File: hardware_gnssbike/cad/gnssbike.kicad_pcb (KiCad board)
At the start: 4 copper layers, 34 x 90 mm, 134 parts, among them J101 HRO TYPE-C-31-M-12, J102 JST SM06B-GHS-TB, J103 JST S4B-ZR-SM4A-TF, J201 Tag-Connect TC2030-NL, J302 Hirose U.FL-R-SMT-1, J401 Hirose FH12-10S-0.5SH(55), J402 Molex 503480-0500, Q401 DMG1012T-7, Q601 DMG1012T-7, Q602 DMG1012T-7, Q603 DMG1012T-7, SW601 XunPu TS-1088R-02026, SW602 XunPu TS-1088R-02026, SW603 XunPu TS-1088R-02026, U101 nPM1300-QEAA, U102 MAX17262REWL, U103 AEM10900, U104 TPS7A0218PDQN, U201 MinewSemi ME54BS13, U301 u-blox MAX-F10S, U302 TI TXU0204BQAR, U501 MX25R6435F, U502 Bosch BMP585, U503 Bosch BMI270, U504 Memsic MMC5603NJ, U505 TI OPT3001DNPR

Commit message: fix(hardware): the antenna cut-out follows the drawing, and the board says which way round
The cut-out was 20,08 mm wide because the data sheet's 15,00 is
asymmetric about the antenna - 2,46 mm one side, 7,54 the other - and
which side was which had not been determined, so 7,54 went on both.

It has now been determined, by measuring the drawings rather than by
reading a line of text, because the data sheet never states it: the wide
side is the side of the "U" printed on top. The "U" is off-centre by
1,10 mm, 22 % of the part's length, and falls on the portion facing the
wide cut-out in two independent figures - the dimension drawing and the
evaluation board. The asymmetry is deliberate: on the 80 x 40 mm
evaluation board the cut-out sits in the middle, 30 mm from one side
edge and 35 from the other, so there was room to centre it and Unictron
did not.

So the cut-out goes back to 15,00 mm, with the wide side toward +x. The
board gets back the 5 mm of ground plane it was giving away, on an
antenna that was already going to sit below its 80 x 40 mm reference
plane. The two strips of copper left in that band are 8,3 and 10,7 mm
instead of 3,2 and 15,9.

And the footprint now carries an orientation mark, which is not
decoration. The part is PHYSICALLY SYMMETRIC - both end terminations are
identical wrap-arounds and the signal terminal is at the geometric
centre - so pick-and-place cannot tell the orientation from the
geometry, and a part placed 180 degrees out puts the wrong side into the
wide cut-out and PASSES every electrical test, because electrically the
two ends are the same. A filled arrow and a "U" on the silkscreen say
which way the logo has to point.

Two things stay open, and both are recorded rather than guessed: the
"U" is Unictron's logo and the data sheet does not declare it as an
orientation mark, so this is a reading of figures; and the data sheet
has no minimum keep-out note at all, referring instead to an application
note, "General guidelines for the 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
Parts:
- moved U302 15.4 mm to (31.5, 33.0)
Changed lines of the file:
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@@
 		(polygon
 			(pts
-				(xy 28.2100 25.0000)
+				(xy 33.2900 25.0000)
 				(xy 48.2900 25.0000)
 				(xy 48.2900 34.8800)
-				(xy 28.2100 34.8800)
+				(xy 33.2900 34.8800)
 			)
 		)
@@
 		(roundrect_rratio 0.25)
 	)
+	(fp_poly
+		(pts (xy 3.10 -1.90) (xy 4.00 -1.40) (xy 3.10 -0.90))
+		(stroke (width 0.12) (type solid))
+		(fill solid)
+		(layer "F.SilkS")
+	)
+	(fp_text user "U"
+		(at 2.20 -2.40 0)
+		(layer "F.SilkS")
+		(effects (font (size 0.6 0.6) (thickness 0.12)))
+	)
 	(model "${KIPRJMOD}/3d/Antena_Unictron_H2UJ4U1H2Q0100_5x3mm.wrl"
 		(offset (xyz 0 0 0))
@@
 		(at 41.5000 35.5000 0)
 		(property "Reference" "JP301"
-			(at 0.0000 -1.1000 0)
+			(at 0.0000 1.1000 0)
 			(layer "F.SilkS")
 			(effects (font (size 0.6 0.6) (thickness 0.12)))
@@
 		(at 40.8000 40.2000 90)
 		(property "Reference" "L301"
-			(at 2.4020 -0.0000 90)
+			(at -0.0000 -1.1500 90)
 			(layer "F.SilkS")
 			(effects (font (size 0.6 0.6) (thickness 0.12)))
@@
 		(at 33.5000 40.3000 180)
 		(property "Reference" "U301"
-			(at 0.0000 5.8000 0)
+			(at -7.1720 5.8000 0)
 			(layer "F.SilkS")
 			(effects (font (size 0.6 0.6) (thickness 0.12)))
@@
 	(footprint "gnssbike:TXU0204_WQFN-14_3x2.5mm_P0.5mm"
 		(layer "F.Cu")
-		(at 44.0000 42.0000 0)
+		(at 31.5000 33.0000 0)
 		(property "Reference" "U302"
-			(at 0.0000 2.1400 0)
+			(at 0.0000 -2.1400 0)
 			(layer "F.SilkS")
 			(effects (font (size 0.6 0.6) (thickness 0.12)))

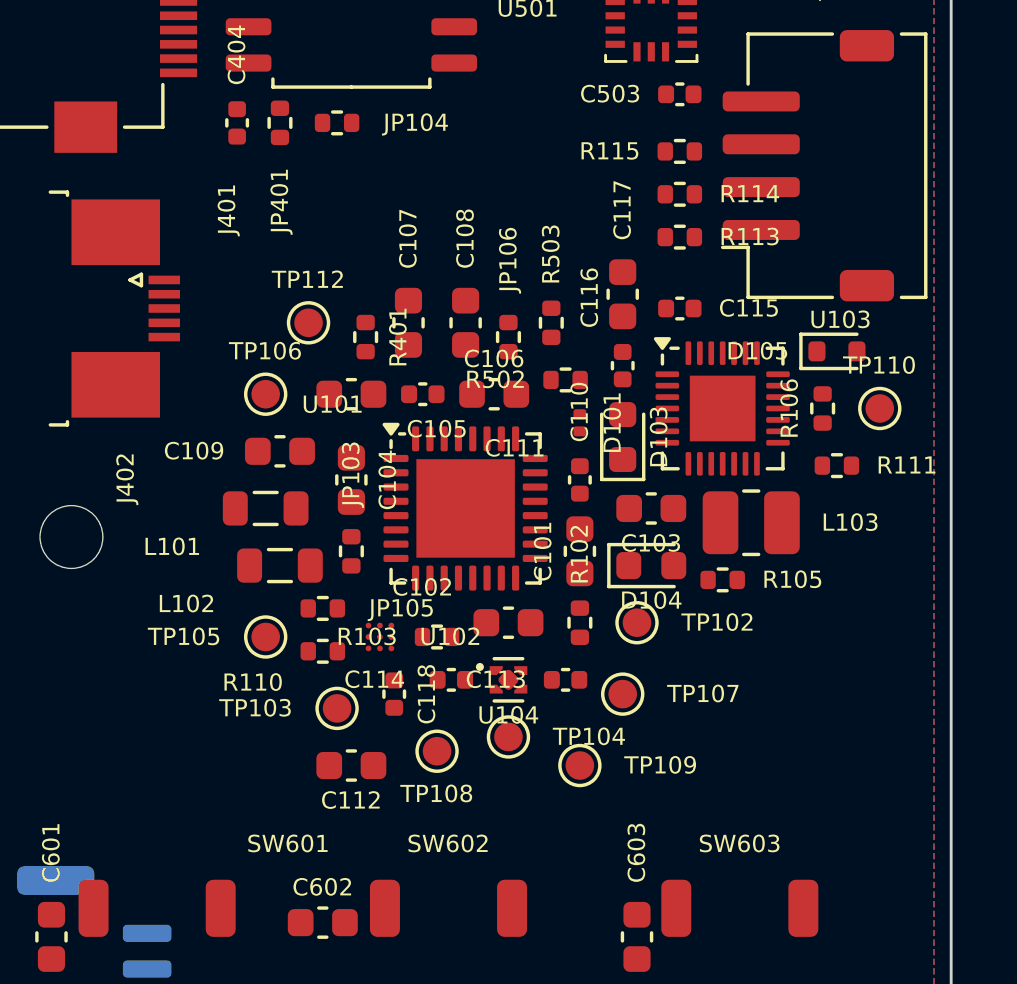
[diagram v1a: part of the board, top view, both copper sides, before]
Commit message: feat(hardware): the solar harvester becomes the ADP5091
The whole e-peas line is zero at LCSC - 31 references, every one of them
- and this board is assembled at JLCPCB. DigiKey never sold the part
either, so consignment was a bet on a part nobody had confirmed is for
sale. The ADP5091ACPZ-2-R7 (C579259) does the same job and can be
bought.

It is not a drop-in. What it does keep: MPPT from 0,08 to 3,3 V, cold
start at 380 mV, a programmable charge threshold, and a programmable
discharge cut-off WITH a switch that really opens between the cell and
the system - which the AEM10900 did not have in that form.

What it loses, and both cost something:

  I2C. There is no bus at all: every threshold is a resistor divider.
  status.solar_mw leaves the screen or becomes an estimate from the net
  current the MAX17262 already measures, and the firmware's aem10900.c,
  361 lines, goes with its binding, its registers and its devicetree
  node.

  The NTC. The AEM10900 cut the charge outside 0 to 45 C by itself, in
  hardware. The ADP5091 has no temperature input at all, and this is
  now an OPEN DEFECT, not a solved problem. The obvious answer - a
  nanoamp comparator on the NTC driving DIS_SW - does not close: the
  divider would be permanently on, and 10 k against 22 k at 4,2 V is
  131 uA continuous, more than the whole device asleep. The four ways
  out are written down where the part is defined.

Three numbers decided the design:

  The inductor is 22 uH +-20 %, not a range - the internal peak control
  was dimensioned for it, and the data sheet says so twice. Isat must be
  30 % above the peak, so >= 390 mA with this variant. The 4,7 uH here
  was the AEM10900's and does not serve; the package grows from
  2,5 x 2,0 to 3 x 3 mm.

  The MPPT ratio is the BOTTOM resistor over the total, and inverting it
  puts the tracker at 0,19 instead of 0,81. 18 M below and 4,3 M above
  give 0,80717 against the 0,807 the panel wants: 0,9 mV of error, in
  E24 values, summing the same 2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
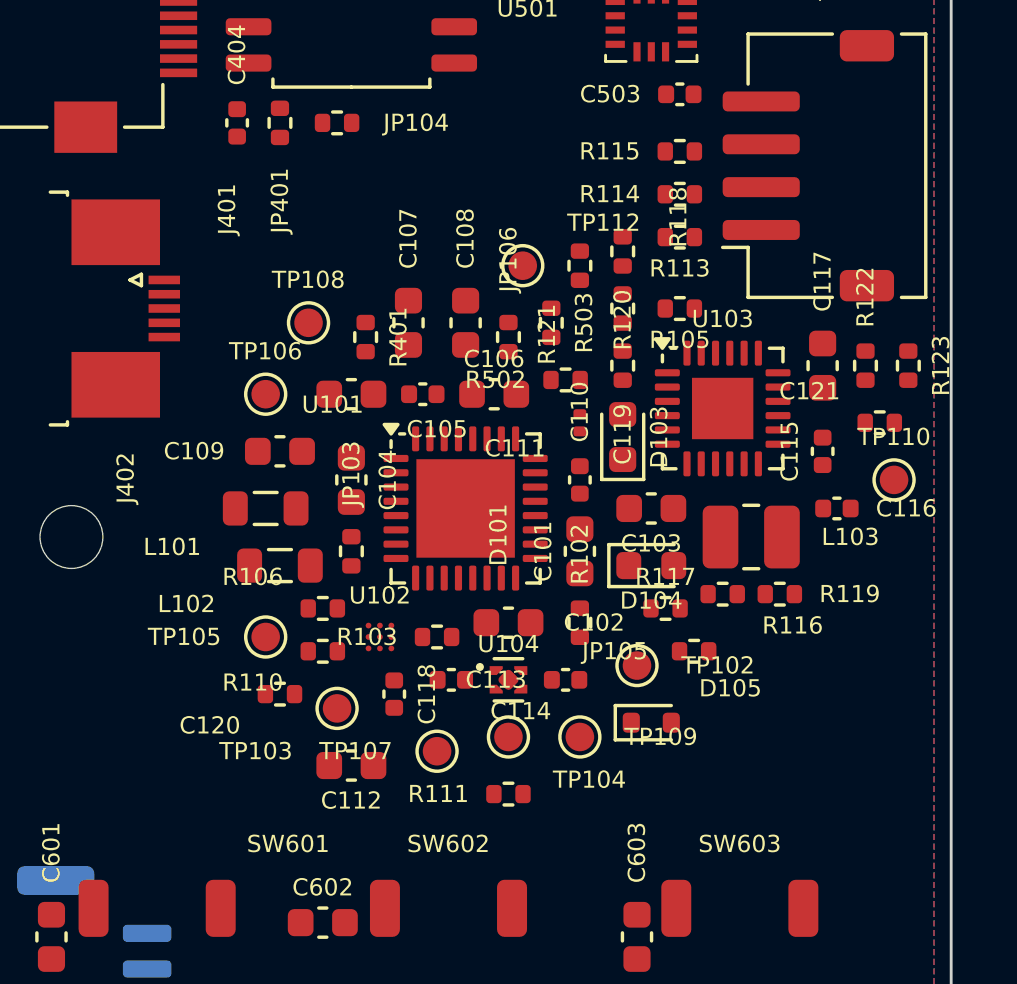
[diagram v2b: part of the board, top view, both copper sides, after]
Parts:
- added C119: 10 nF, Resistor_SMD:R_0402_1005Metric, F.Cu at (47.5, 64.0)
- added C120: 100 nF, Resistor_SMD:R_0402_1005Metric, F.Cu at (35.5, 75.5)
- added C121: 4,7 uF, Resistor_SMD:R_0402_1005Metric, F.Cu at (56.5, 66.0)
- added R116: 18 M, Resistor_SMD:R_0402_1005Metric, F.Cu at (51.0, 72.0)
- added R117: 4,3 M, Resistor_SMD:R_0402_1005Metric, F.Cu at (49.0, 72.5)
- added R118: 4,32 M, Resistor_SMD:R_0402_1005Metric, F.Cu at (47.5, 62.0)
- added R119: 2,67 M, Resistor_SMD:R_0402_1005Metric, F.Cu at (53.0, 72.0)
- added R120: 6,65 M, Resistor_SMD:R_0402_1005Metric, F.Cu at (47.5, 60.0)
- added R121: 3,32 M, Resistor_SMD:R_0402_1005Metric, F.Cu at (46.0, 60.5)
- added R122: 402 k, Resistor_SMD:R_0402_1005Metric, F.Cu at (56.0, 64.0)
- added R123: 111 k, Resistor_SMD:R_0402_1005Metric, F.Cu at (57.5, 64.0)
- L103: value 4,7 uH -> 22 uH
- U103: value AEM10900 -> ADP5091ACPZ-2; footprint Package_DFN_QFN:QFN-28-1EP_4x4mm_P0.4mm_EP2.3x2.3mm -> Package_DFN_QFN:QFN-24-1EP_4x4mm_P0.5mm_EP2.15x2.15mm
- moved R106 18.8 mm to (37.0, 72.5), turned to 0 degrees
- moved R111 16.3 mm to (43.5, 79.0)
- moved TP108 15.7 mm to (36.5, 62.5)
- moved D105 14.5 mm to (48.5, 76.5)
- moved JP105 13.1 mm to (50.0, 74.0)
- moved R105 9.62 mm to (49.5, 62.0)
- moved C116 9.01 mm to (55.0, 69.0), turned to 0 degrees
- moved TP112 7.76 mm to (44.0, 60.5)
- moved C117 7.43 mm to (54.5, 64.0)
- moved C115 7.07 mm to (54.5, 67.0), turned to 90 degrees
- moved TP107 6.80 mm to (41.0, 77.5)
- moved TP110 2.55 mm to (57.0, 68.0)
- moved TP102 1.50 mm to (48.0, 74.5)
- moved TP109 1.00 mm to (46.0, 77.0)
- moved L103 0.50 mm to (52.0, 70.0)
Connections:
- C116 pad 1: VINT -> (no net)
- R104 pad 2: DIS_STO_CH -> DIS_SW
- R105 pad 1: DIS_STO_CH -> DIS_SW
- R106 pad 1: TH_REF -> (no net)
- R106 pad 2: TH_MON -> NTC_SOLAR
- R111 pad 2: IRQ_AEM -> IRQ_LIVRE
- RT101 pad 1: TH_MON -> NTC_SOLAR
- TP110 pad 1: VINT -> SRC
- U103 pad 1: GND -> (no net)
- U103 pad 10: 3V0 -> GND
- U103 pad 11: IRQ_AEM -> (no net)
- U103 pad 12: PWR_SCL -> GND
- U103 pad 13: PWR_SDA -> SW_DCDC
- U103 pad 14: VINT -> REG_OUT
- U103 pad 15: VINT -> REG_OUT
- U103 pad 16: VINT -> VBAT_SYS
- U103 pad 17: GND -> VBAT_SYS
- U103 pad 18: VINT -> (no net)
- U103 pad 19: VINT -> (no net)
- U103 pad 20: VINT -> VID
- U103 pad 21: VINT -> MINOP
- U103 pad 22: VINT -> DIS_SW
- U103 pad 24: VINT -> GND
- U103 pad 25: TH_MON -> GND
- U103 pad 3: (no net) -> GND
- U103 pad 4: GND -> SETSD
- U103 pad 5: SW_DCDC -> (no net)
- U103 pad 6: VINT -> TERM
- U103 pad 7: (no net) -> MPPT
- U103 pad 8: (no net) -> CBP
- U103 pad 9: DIS_STO_CH -> SRC
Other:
- board text added: "144 pecas colocadas, 7 fora da placa (painel, antena e modulos solares vivem na caixa)"
- board text removed: "133 pecas colocadas, 7 fora da placa (painel, antena e modulos solares vivem na caixa)"

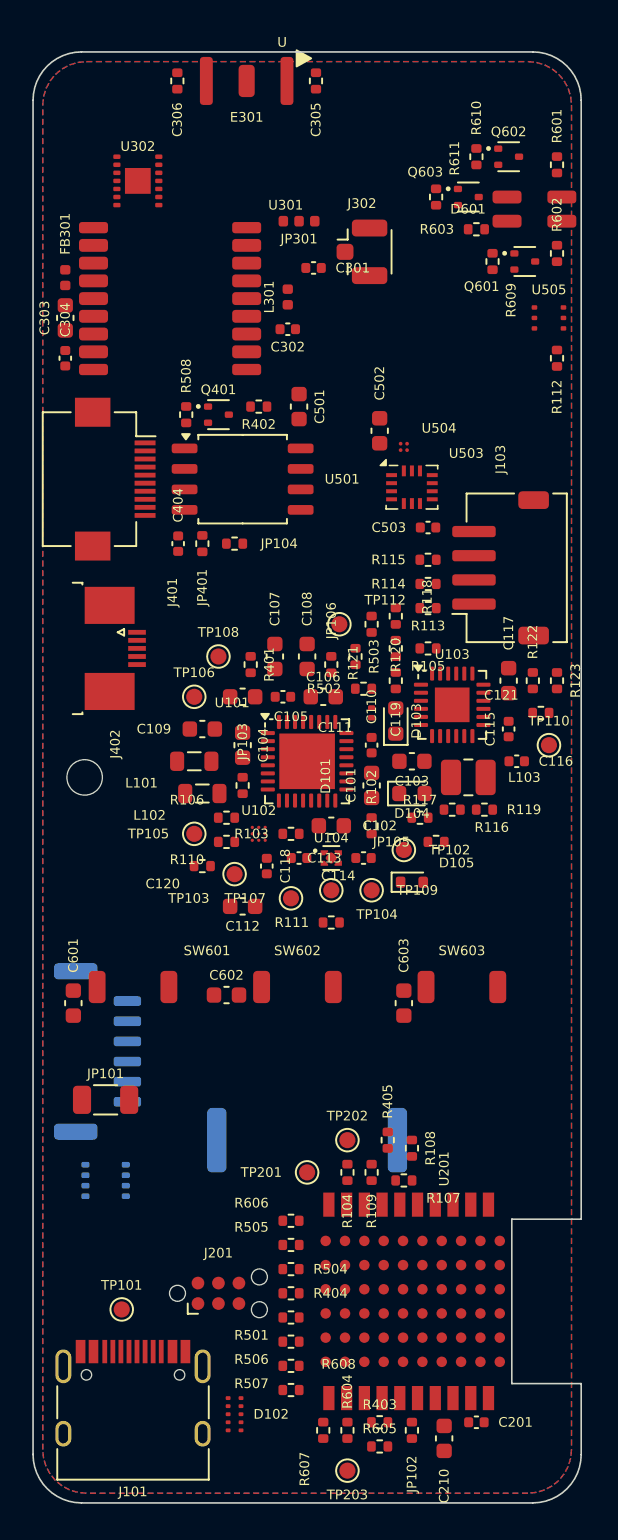
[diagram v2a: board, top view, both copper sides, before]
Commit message: fix(hardware): the router measures copper to the edge, not centre lines
The DRC found two errors on the routed board: a GND track 0,100 mm from
the board outline and a stitching via 0,075 mm from it, against the
0,300 mm the board setup asks for.

The cause was in the grid, and it was a category mistake rather than a
wrong number. BORDA_COBRE is the clearance the DRC wants between COPPER
and the outline, but what sits on a grid point is a CENTRE LINE. A via
of 0,45 mm centred 0,3 mm from the edge leaves copper at 0,075, and the
router drops a via wherever it changes layer, so every grid point has to
hold the widest thing that can land on it - the via, not the track.

The margin is now BORDA_COBRE plus half a via, 0,525 mm, and it applies
to the outline, to the rounded corners and to the milled notch under the
radio module's antenna, which is board edge too.

It costs 0,225 mm of routable area all round and one routed connection:
150 instead of 151, with 955 segments and 448 vias.

The board now passes the KiCad DRC with 0 violations and 0 unconnected
items, and 18 of the datasheet rules are measured and met. The one that
is not is US1: the USB differential pair is still unrouted and needs
hand finishing at 0,352 mm, which is recorded.
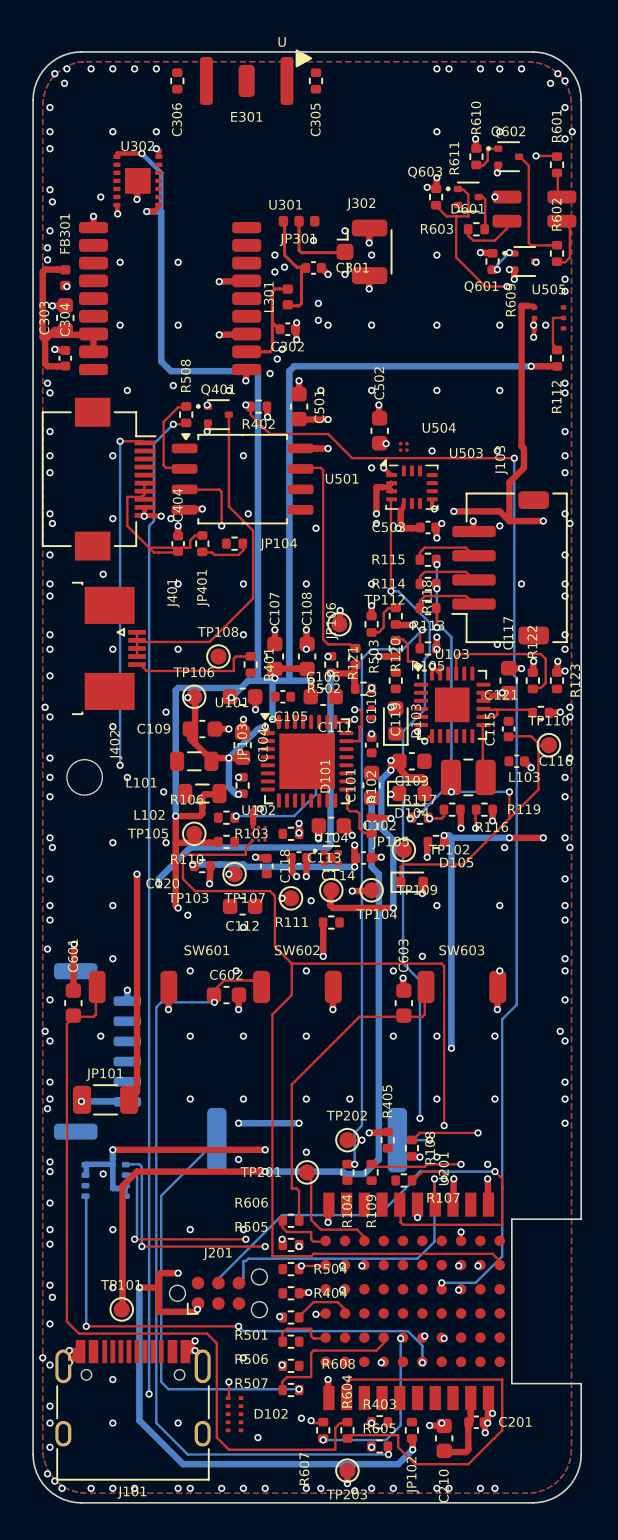
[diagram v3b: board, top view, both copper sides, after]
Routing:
- net 3V0: track 0.00 -> 217.3 mm, vias 0 -> 18
- net 3V0_SENS: track 0.00 -> 116.6 mm, vias 0 -> 13
- net DISP_SCK: track 0.00 -> 89.0 mm, vias 0 -> 3
- net RGB_B: track 0.00 -> 80.6 mm, vias 0 -> 2
- net VSYS: track 0.00 -> 78.7 mm, vias 0 -> 5
- net NOR_MISO: track 0.00 -> 76.8 mm, vias 0 -> 3
- net PWR_SDA: track 0.00 -> 75.8 mm, vias 0 -> 2
- net BL_PWM: track 0.00 -> 75.6 mm, vias 0 -> 4
- net SD3V0: track 0.00 -> 69.4 mm, vias 0 -> 4
- net GND: track 0.00 -> 66.3 mm, vias 0 -> 310
- net CC1: track 0.00 -> 62.8 mm, vias 0 -> 2
- net IMU_INT: track 0.00 -> 57.6 mm, vias 0 -> 3
- net VBAT_SYS: track 0.00 -> 54.5 mm, vias 0 -> 7
- net 1V8: track 0.00 -> 49.7 mm, vias 0 -> 5
- net KEY_C_SW: track 0.00 -> 49.2 mm, vias 0 -> 2
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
